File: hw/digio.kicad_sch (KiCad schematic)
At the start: 11 parts, among them U17 SN74LVC2T45DCUR

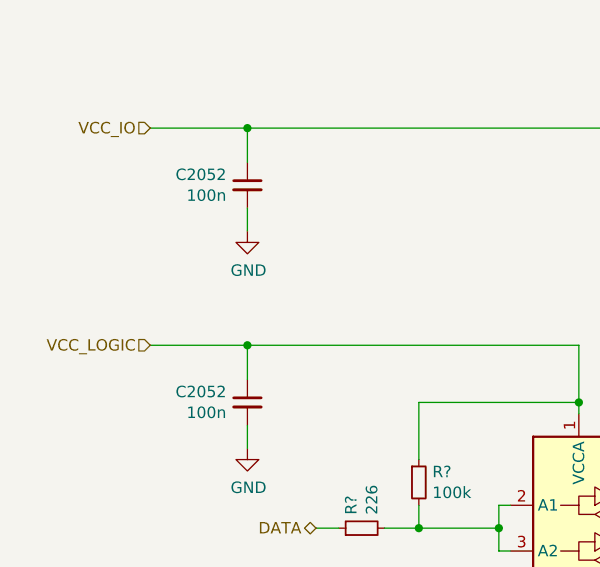
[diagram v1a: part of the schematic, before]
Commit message: Modifications to power-supply: noise improvements
- DNL C12 (cap between 5V input and -2V5); created a bypass for noise
  coming into 5V. Improved spectrum up to ~200kHz, reducing spurs.
- Enabled C14 (feedback-zero for -2V5 regulator); reduce spurs (unstabilities?)
- DNL C145 (1u cap after ferrite bead isolating Vpp_analog.
- Replaced Vpp_analog isolation FB1 by a 10k resistor (R126)

The bead FB1 behaves as an 2uH inductor at low freq. The LC filter
formed by FB1 and decoupling caps is drastically underdamped by the
weak load (only analog switches) and enhances noise in the 10k-200k
band (depending on caps; particularly bad if C145 is loaded).
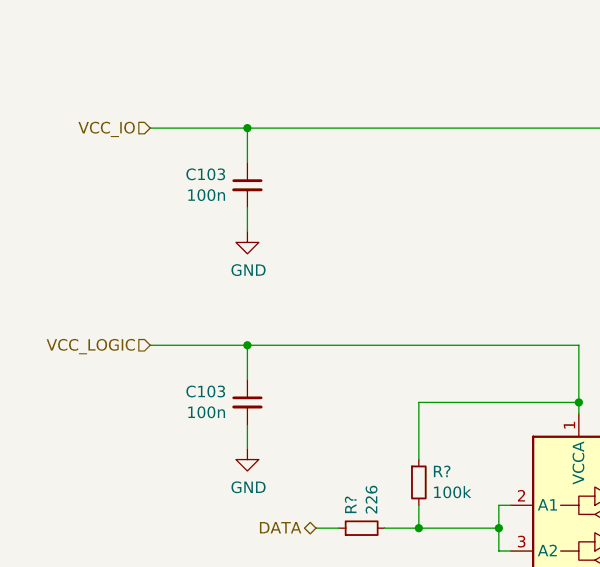
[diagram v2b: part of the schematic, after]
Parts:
- renumbered C2052 to C103
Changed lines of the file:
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@@
 		(on_board yes)
 		(dnp no)
-		(property "Reference" "C2052"
+		(property "Reference" "C103"
 			(at 79.5782 80.7466 0)
 			(effects
@@
 		(on_board yes)
 		(dnp no)
-		(property "Reference" "C2052"
+		(property "Reference" "C103"
 			(at 79.5782 56.6166 0)
 			(effects

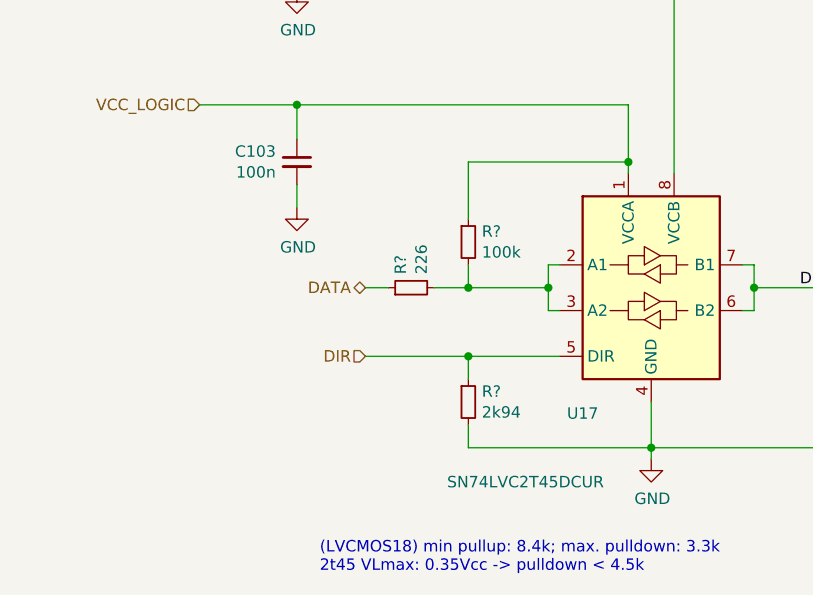
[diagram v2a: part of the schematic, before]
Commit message: added pll clock in divider from BNC, several pull-resistors
pull-resistors permit distinguishing board revisions.
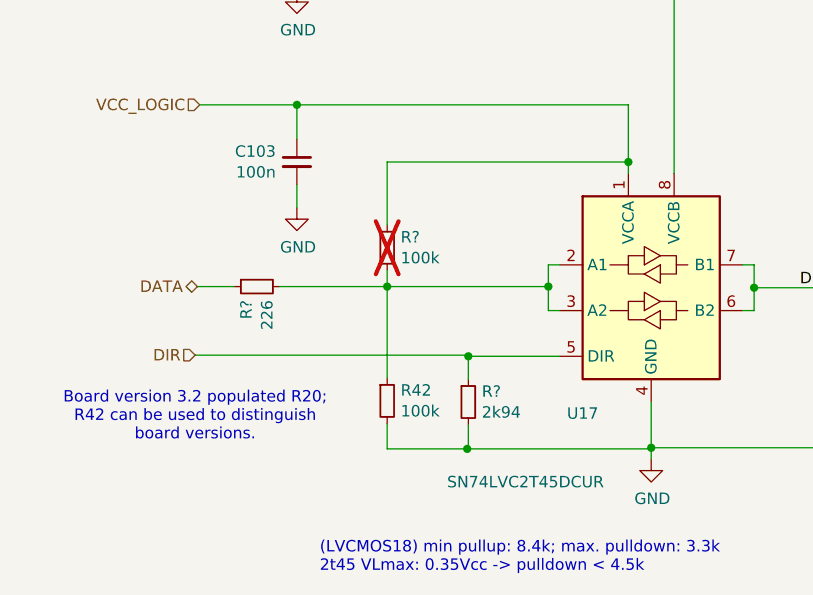
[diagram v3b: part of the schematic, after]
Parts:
- added R42: 100k, Resistor_SMD:R_0603_1608Metric, symbol Device:R_Small
- R?: now not fitted
- U17: footprint Package_SO:VSSOP-8_2.4x2.1mm_P0.5mm -> Package_SO:VSSOP-8_2.3x2mm_P0.5mm
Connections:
- net GND: now also R42.2
- net at R?.2, R?.2, U17.2 (A1)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: now also R42.1
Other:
- note added: "Board version 3.2 populated R20; R42 can be used to distinguish board versions."
- moved on the sheet: R?
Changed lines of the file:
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@@
 	(paper "A4")
 	(junction
-		(at 100.965 95.885)
+		(at 109.855 95.758)
 		(diameter 0)
 		(color 0 0 0 0)
@@
 	)
 	(junction
-		(at 109.855 95.885)
+		(at 100.838 113.792)
 		(diameter 0)
 		(color 0 0 0 0)
@@
 	)
 	(junction
+		(at 91.948 95.758)
+		(diameter 0)
+		(color 0 0 0 0)
+	)
+	(junction
 		(at 81.915 75.565)
 		(diameter 0)
@@
 	(wire
 		(pts
-			(xy 109.855 93.345) (xy 109.855 95.885)
+			(xy 109.855 93.345) (xy 109.855 95.758)
 		)
 		(stroke
@@
 	(wire
 		(pts
-			(xy 97.155 95.885) (xy 100.965 95.885)
+			(xy 80.01 95.758) (xy 91.948 95.758)
 		)
 		(stroke
@@
 	(wire
 		(pts
-			(xy 100.965 88.265) (xy 100.965 81.915)
-		)
-		(stroke
-			(width 0)
-			(type default)
-		)
-	)
-	(wire
-		(pts
-			(xy 100.965 113.665) (xy 121.285 113.665)
+			(xy 91.948 88.9) (xy 91.948 81.915)
+		)
+		(stroke
+			(width 0)
+			(type default)
+		)
+	)
+	(wire
+		(pts
+			(xy 100.838 113.538) (xy 100.965 113.538)
 		)
 		(stroke
@@
 	(wire
 		(pts
+			(xy 100.838 113.792) (xy 121.158 113.792)
+		)
+		(stroke
+			(width 0)
+			(type default)
+		)
+	)
+	(wire
+		(pts
 			(xy 173.355 102.235) (xy 173.355 95.885)
 		)
@@
 	(wire
 		(pts
+			(xy 100.965 113.538) (xy 100.965 111.125)
+		)
+		(stroke
+			(width 0)
+			(type default)
+		)
+	)
+	(wire
+		(pts
 			(xy 109.855 98.425) (xy 111.125 98.425)
 		)
@@
 	(wire
 		(pts
-			(xy 100.965 95.885) (xy 109.855 95.885)
-		)
-		(stroke
-			(width 0)
-			(type default)
-		)
-	)
-	(wire
-		(pts
 			(xy 182.245 95.885) (xy 193.675 95.885)
 		)
@@
 	(wire
 		(pts
-			(xy 89.535 103.505) (xy 100.965 103.505)
-		)
-		(stroke
-			(width 0)
-			(type default)
-		)
-	)
-	(wire
-		(pts
-			(xy 100.965 111.125) (xy 100.965 113.665)
+			(xy 70.612 103.378) (xy 100.965 103.378)
+		)
+		(stroke
+			(width 0)
+			(type default)
+		)
+	)
+	(wire
+		(pts
+			(xy 100.838 113.538) (xy 100.838 113.792)
 		)
 		(stroke
@@
 	(wire
 		(pts
+			(xy 91.948 95.758) (xy 109.855 95.758)
+		)
+		(stroke
+			(width 0)
+			(type default)
+		)
+	)
+	(wire
+		(pts
 			(xy 161.925 113.665) (xy 161.925 107.315)
 		)
@@
 	(wire
 		(pts
+			(xy 121.158 113.792) (xy 121.158 113.665)
+		)
+		(stroke
+			(width 0)
+			(type default)
+		)
+	)
+	(wire
+		(pts
 			(xy 100.965 103.505) (xy 111.125 103.505)
 		)
@@
 	(wire
 		(pts
+			(xy 91.948 113.792) (xy 100.838 113.792)
+		)
+		(stroke
+			(width 0)
+			(type default)
+		)
+	)
+	(wire
+		(pts
+			(xy 91.948 110.998) (xy 91.948 113.792)
+		)
+		(stroke
+			(width 0)
+			(type default)
+		)
+	)
+	(wire
+		(pts
 			(xy 198.755 100.965) (xy 198.755 104.775)
 		)
@@
 	(wire
 		(pts
-			(xy 109.855 95.885) (xy 109.855 98.425)
-		)
-		(stroke
-			(width 0)
-			(type default)
-		)
-	)
-	(wire
-		(pts
-			(xy 100.965 81.915) (xy 118.745 81.915)
+			(xy 91.948 105.918) (xy 91.948 95.758)
+		)
+		(stroke
+			(width 0)
+			(type default)
+		)
+	)
+	(wire
+		(pts
+			(xy 100.965 103.378) (xy 100.965 103.505)
+		)
+		(stroke
+			(width 0)
+			(type default)
+		)
+	)
+	(wire
+		(pts
+			(xy 91.948 81.915) (xy 118.745 81.915)
 		)
 		(stroke
@@
 	(wire
 		(pts
-			(xy 100.965 93.345) (xy 100.965 95.885)
+			(xy 91.948 93.98) (xy 91.948 95.758)
 		)
 		(stroke
@@
 	(wire
 		(pts
-			(xy 89.535 95.885) (xy 92.075 95.885)
-		)
-		(stroke
-			(width 0)
-			(type default)
-		)
-	)
-	(wire
-		(pts
 			(xy 109.855 93.345) (xy 111.125 93.345)
 		)
@@
 	(wire
 		(pts
+			(xy 70.866 95.758) (xy 74.93 95.758)
+		)
+		(stroke
+			(width 0)
+			(type default)
+		)
+	)
+	(wire
+		(pts
 			(xy 100.965 103.505) (xy 100.965 106.045)
 		)
@@
 	(wire
 		(pts
+			(xy 121.158 113.665) (xy 121.285 113.665)
+		)
+		(stroke
+			(width 0)
+			(type default)
+		)
+	)
+	(wire
+		(pts
 			(xy 121.285 113.665) (xy 121.285 114.935)
 		)
@@
 	(wire
 		(pts
+			(xy 109.855 95.758) (xy 109.855 98.425)
+		)
+		(stroke
+			(width 0)
+			(type default)
+		)
+	)
+	(wire
+		(pts
 			(xy 81.915 51.435) (xy 81.915 55.245)
 		)
@@
 			(width 0)
 			(type default)
+		)
+	)
+	(text "Board version 3.2 populated R20;\nR42 can be used to distinguish\nboard versions."
+		(exclude_from_sim no)
+		(at 70.612 110.236 0)
+		(effects
+			(font
+				(size 1.27 1.27)
+			)
 		)
 	)
@@
 	(hierarchical_label "DIR"
 		(shape input)
-		(at 89.535 103.505 180)
+		(at 70.612 103.378 180)
 		(effects
 			(font
@@
 	(hierarchical_label "DATA"
 		(shape bidirectional)
-		(at 89.535 95.885 180)
+		(at 70.866 95.758 180)
 		(effects
 			(font
@@
 			)
 		)
-		(property "Footprint" "Package_SO:VSSOP-8_2.4x2.1mm_P0.5mm"
+		(property "Footprint" "Package_SO:VSSOP-8_2.3x2mm_P0.5mm"
 			(at 122.555 109.855 0)
 			(effects
@@
 	(symbol
 		(lib_id "Device:R_Small")
-		(at 94.615 95.885 90)
+		(at 77.47 95.758 90)
+		(mirror x)
 		(unit 1)
 		(exclude_from_sim no)
@@
 		(dnp no)
 		(property "Reference" "R?"
-			(at 93.4466 94.3864 0)
+			(at 76.3016 97.2566 0)
 			(effects
 				(font
@@
 		)
 		(property "Value" "226"
-			(at 95.758 94.3864 0)
+			(at 78.613 97.2566 0)
 			(effects
 				(font
@@
 		)
 		(property "Footprint" "Resistor_SMD:R_0603_1608Metric"
-			(at 94.615 95.885 0)
+			(at 77.47 95.758 0)
 			(effects
 				(font
@@
 		)
 		(property "Datasheet" "~"
-			(at 94.615 95.885 0)
+			(at 77.47 95.758 0)
 			(effects
 				(font
@@
 		)
 		(property "Description" ""
-			(at 94.615 95.885 0)
+			(at 77.47 95.758 0)
 			(effects
 				(font
@@
 	(symbol
 		(lib_id "Device:R_Small")
+		(at 91.948 108.458 0)
+		(unit 1)
+		(exclude_from_sim no)
+		(in_bom yes)
+		(on_board yes)
+		(dnp no)
+		(property "Reference" "R42"
+			(at 93.4466 107.2896 0)
+			(effects
+				(font
+					(size 1.27 1.27)
+				)
+				(justify left)
+			)
+		)
+		(property "Value" "100k"
+			(at 93.4466 109.601 0)
+			(effects
+				(font
+					(size 1.27 1.27)
+				)
+				(justify left)
+			)
+		)
+		(property "Footprint" "Resistor_SMD:R_0603_1608Metric"
+			(at 91.948 108.458 0)
+			(effects
+				(font
+					(size 1.27 1.27)
+				)
+				(hide yes)
+			)
+		)
+		(property "Datasheet" "~"
+			(at 91.948 108.458 0)
+			(effects
+				(font
+					(size 1.27 1.27)
+				)
+				(hide yes)
+			)
+		)
+		(property "Description" ""
+			(at 91.948 108.458 0)
+			(effects
+				(font
+					(size 1.27 1.27)
+				)
+				(hide yes)
+			)
+		)
+		(pin "1"
+		)
+		(pin "2"
+		)
+		(instances
+			(project "usbadc"
+				(path "/7c8a1f8d-8834-4c9b-aaae-1f231e9b09a1/39acc7d1-a995-4616-8037-aaf3c117cf9c"
+					(reference "R42")
+					(unit 1)
+				)
+			)
+		)
+	)
+	(symbol
+		(lib_id "Device:R_Small")
 		(at 179.705 95.885 90)
 		(unit 1)
@@
 	(symbol
 		(lib_id "Device:R_Small")
-		(at 100.965 90.805 0)
+		(at 91.948 91.44 0)
 		(unit 1)
 		(exclude_from_sim no)
 		(in_bom yes)
 		(on_board yes)
-		(dnp no)
+		(dnp yes)
 		(property "Reference" "R?"
-			(at 102.4636 89.6366 0)
+			(at 93.4466 90.2716 0)
 			(effects
 				(font
@@
 		)
 		(property "Value" "100k"
-			(at 102.4636 91.948 0)
+			(at 93.4466 92.583 0)
 			(effects
 				(font
@@
 		)
 		(property "Footprint" "Resistor_SMD:R_0603_1608Metric"
-			(at 100.965 90.805 0)
+			(at 91.948 91.44 0)
 			(effects
 				(font
@@
 		)
 		(property "Datasheet" "~"
-			(at 100.965 90.805 0)
+			(at 91.948 91.44 0)
 			(effects
 				(font
@@
 		)
 		(property "Description" ""
-			(at 100.965 90.805 0)
-			(effects
-				(font
+			(at 91.948 91.44 0)
+			(effects
+				(font

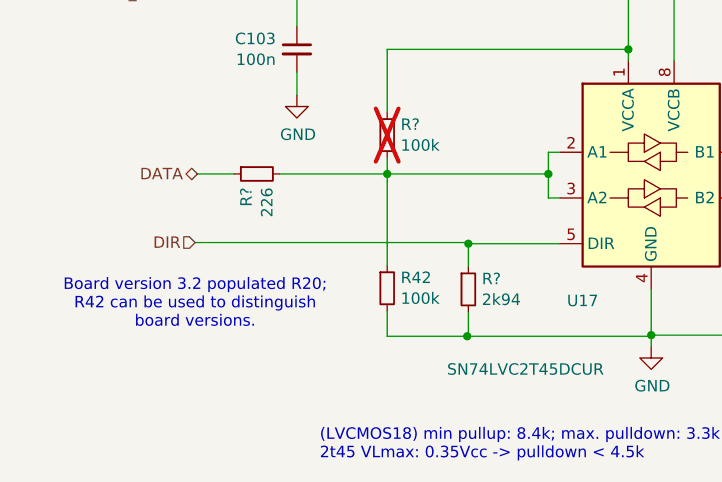
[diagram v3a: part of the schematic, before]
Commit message: moved board-version resistors to SPI interface
GPIO driver should always be IN (i.e., driving the fpga); thus
a pull-resistor at that point is useless.
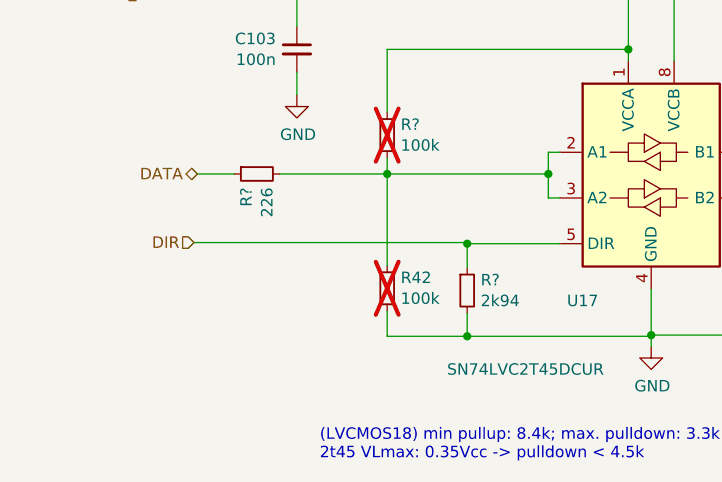
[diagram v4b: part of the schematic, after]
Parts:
- R42: now not fitted
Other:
- note removed: "Board version 3.2 populated R20; R42 can be used to distinguish board versions."
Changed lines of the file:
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@@
 	(paper "A4")
+	(junction
+		(at 100.838 103.505)
+		(diameter 0)
+		(color 0 0 0 0)
+	)
 	(junction
 		(at 109.855 95.758)
@@
 	)
 	(junction
-		(at 100.965 103.505)
-		(diameter 0)
-		(color 0 0 0 0)
-	)
-	(junction
 		(at 118.745 81.915)
 		(diameter 0)
@@
 	(wire
 		(pts
-			(xy 100.838 113.538) (xy 100.965 113.538)
-		)
-		(stroke
-			(width 0)
-			(type default)
-		)
-	)
-	(wire
-		(pts
 			(xy 173.355 107.315) (xy 173.355 113.665)
 		)
@@
 	(wire
 		(pts
-			(xy 100.965 113.538) (xy 100.965 111.125)
+			(xy 100.838 111.252) (xy 100.838 113.792)
 		)
 		(stroke
@@
 	(wire
 		(pts
-			(xy 70.612 103.378) (xy 100.965 103.378)
-		)
-		(stroke
-			(width 0)
-			(type default)
-		)
-	)
-	(wire
-		(pts
-			(xy 100.838 113.538) (xy 100.838 113.792)
+			(xy 70.485 103.378) (xy 100.838 103.378)
 		)
 		(stroke
@@
 	(wire
 		(pts
+			(xy 100.838 103.505) (xy 111.125 103.505)
+		)
+		(stroke
+			(width 0)
+			(type default)
+		)
+	)
+	(wire
+		(pts
 			(xy 91.948 95.758) (xy 109.855 95.758)
 		)
@@
 	(wire
 		(pts
-			(xy 100.965 103.505) (xy 111.125 103.505)
-		)
-		(stroke
-			(width 0)
-			(type default)
-		)
-	)
-	(wire
-		(pts
 			(xy 91.948 113.792) (xy 100.838 113.792)
 		)
@@
 	(wire
 		(pts
-			(xy 100.965 103.378) (xy 100.965 103.505)
+			(xy 100.838 103.378) (xy 100.838 103.505)
 		)
 		(stroke
@@
 	(wire
 		(pts
-			(xy 100.965 103.505) (xy 100.965 106.045)
+			(xy 100.838 103.505) (xy 100.838 106.172)
 		)
 		(stroke
@@
 			(width 0)
 			(type default)
-		)
-	)
-	(text "Board version 3.2 populated R20;\nR42 can be used to distinguish\nboard versions."
-		(exclude_from_sim no)
-		(at 70.612 110.236 0)
-		(effects
-			(font
-				(size 1.27 1.27)
-			)
 		)
 	)
@@
 	(hierarchical_label "DIR"
 		(shape input)
-		(at 70.612 103.378 180)
+		(at 70.485 103.378 180)
 		(effects
 			(font
@@
 		(in_bom yes)
 		(on_board yes)
-		(dnp no)
+		(dnp yes)
 		(property "Reference" "R42"
 			(at 93.4466 107.2896 0)
@@
 	(symbol
 		(lib_id "Device:R_Small")
-		(at 100.965 108.585 0)
+		(at 100.838 108.712 0)
 		(unit 1)
 		(exclude_from_sim no)
@@
 		(dnp no)
 		(property "Reference" "R?"
-			(at 102.4636 107.4166 0)
+			(at 102.3366 107.5436 0)
 			(effects
 				(font
@@
 		)
 		(property "Value" "2k94"
-			(at 102.4636 109.728 0)
+			(at 102.3366 109.855 0)
 			(effects
 				(font
@@
 		)
 		(property "Footprint" "Resistor_SMD:R_0603_1608Metric"
-			(at 100.965 108.585 0)
+			(at 100.838 108.712 0)
 			(effects
 				(font
@@
 		)
 		(property "Datasheet" "~"
-			(at 100.965 108.585 0)
+			(at 100.838 108.712 0)
 			(effects
 				(font
@@
 		)
 		(property "Description" ""
-			(at 100.965 108.585 0)
-			(effects
-				(font
+			(at 100.838 108.712 0)
+			(effects
+				(font

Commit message: updated parts assignments
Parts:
- R42, R? (x2): Manufacturer (none) -> Stackpole; Part (none) -> RMCF0603FT100K
- R?: Manufacturer (none) -> Stackpole; Part (none) -> RMCF0603FT226R
- R?: Manufacturer (none) -> Stackpole; Part (none) -> RMCF0603FT33R0
- R?: Manufacturer (none) -> Stackpole; Part (none) -> RMCF0603FT2K94
- U17: Manufacturer (none) -> Nexperia; Part (none) -> 74LVC2T45DC,125
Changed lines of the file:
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@@
 			)
 		)
-		(property "Datasheet" " ~"
+		(property "Datasheet" "~"
 			(at 198.755 95.885 0)
 			(effects
@@
 		)
 		(property "Description" ""
+			(at 121.285 95.885 0)
+			(effects
+				(font
+					(size 1.27 1.27)
+				)
+				(hide yes)
+			)
+		)
+		(property "Manufacturer" "Nexperia"
+			(at 121.285 95.885 0)
+			(effects
+				(font
+					(size 1.27 1.27)
+				)
+				(hide yes)
+			)
+		)
+		(property "Part" "74LVC2T45DC,125"
 			(at 121.285 95.885 0)
 			(effects
@@
 			)
 		)
+		(property "Manufacturer" "Stackpole"
+			(at 77.47 95.758 0)
+			(effects
+				(font
+					(size 1.27 1.27)
+				)
+				(hide yes)
+			)
+		)
+		(property "Part" "RMCF0603FT226R"
+			(at 77.47 95.758 0)
+			(effects
+				(font
+					(size 1.27 1.27)
+				)
+				(hide yes)
+			)
+		)
 		(pin "1"
 		)
@@
 			)
 		)
+		(property "Manufacturer" "Stackpole"
+			(at 91.948 108.458 0)
+			(effects
+				(font
+					(size 1.27 1.27)
+				)
+				(hide yes)
+			)
+		)
+		(property "Part" "RMCF0603FT100K"
+			(at 91.948 108.458 0)
+			(effects
+				(font
+					(size 1.27 1.27)
+				)
+				(hide yes)
+			)
+		)
 		(pin "1"
 		)
@@
 			)
 		)
+		(property "Manufacturer" "Stackpole"
+			(at 179.705 95.885 0)
+			(effects
+				(font
+					(size 1.27 1.27)
+				)
+				(hide yes)
+			)
+		)
+		(property "Part" "RMCF0603FT33R0"
+			(at 179.705 95.885 0)
+			(effects
+				(font
+					(size 1.27 1.27)
+				)
+				(hide yes)
+			)
+		)
 		(pin "1"
 		)
@@
 			)
 		)
+		(property "Manufacturer" "Stackpole"
+			(at 100.838 108.712 0)
+			(effects
+				(font
+					(size 1.27 1.27)
+				)
+				(hide yes)
+			)
+		)
+		(property "Part" "RMCF0603FT2K94"
+			(at 100.838 108.712 0)
+			(effects
+				(font
+					(size 1.27 1.27)
+				)
+				(hide yes)
+			)
+		)
 		(pin "1"
 		)
@@
 			)
 		)
+		(property "Manufacturer" "Stackpole"
+			(at 173.355 104.775 0)
+			(effects
+				(font
+					(size 1.27 1.27)
+				)
+				(hide yes)
+			)
+		)
+		(property "Part" "RMCF0603FT100K"
+			(at 173.355 104.775 0)
+			(effects
+				(font
+					(size 1.27 1.27)
+				)
+				(hide yes)
+			)
+		)
 		(pin "1"
 		)
@@
 			(at 91.948 91.44 0)
 			(effects
+				(font
+					(size 1.27 1.27)
+				)
+				(hide yes)
+			)
+		)
+		(property "Manufacturer" "Stackpole"
+			(at 91.948 91.44 0)
+			(effects
+				(font
+					(size 1.27 1.27)
+				)
+				(hide yes)
+			)
+		)
+		(property "Part" "RMCF0603FT100K"
+			(at 91.948 91.44 0)
+			(effects
